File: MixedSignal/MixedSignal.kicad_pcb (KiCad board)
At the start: 4 copper layers, 103 x 75.5 mm, 106 parts, among them J1 PPPC202LFBN-RC, J2 PPPC202LFBN-RC, J4 Input Audio Jack, J5 SDS-50J, U1 ADG734, U10 ADG734, U10LDO1 TPS7A4901DGNR, U11 ADCMP602BRMZ, U12 ADCMP602BRMZ, U13 ADCMP602BRMZ, U14 ADCMP602BRMZ, U15 ADCMP602BRMZ, U16 ADCMP602BRMZ, U17 ADCMP602BRMZ, U18 CDCLVC1108PW, U19 DS90LV012ATMFX, U2 ADG734, U20 AP2112K-3.3TRG1, U3 ADG734, U4 WE-TVS-82400102 TVS Diode Arr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, U5 OPA1612AxD, U8 REF5025AD, U9 OPA1612AxD, U9LDO1 TPS7A3001DGN

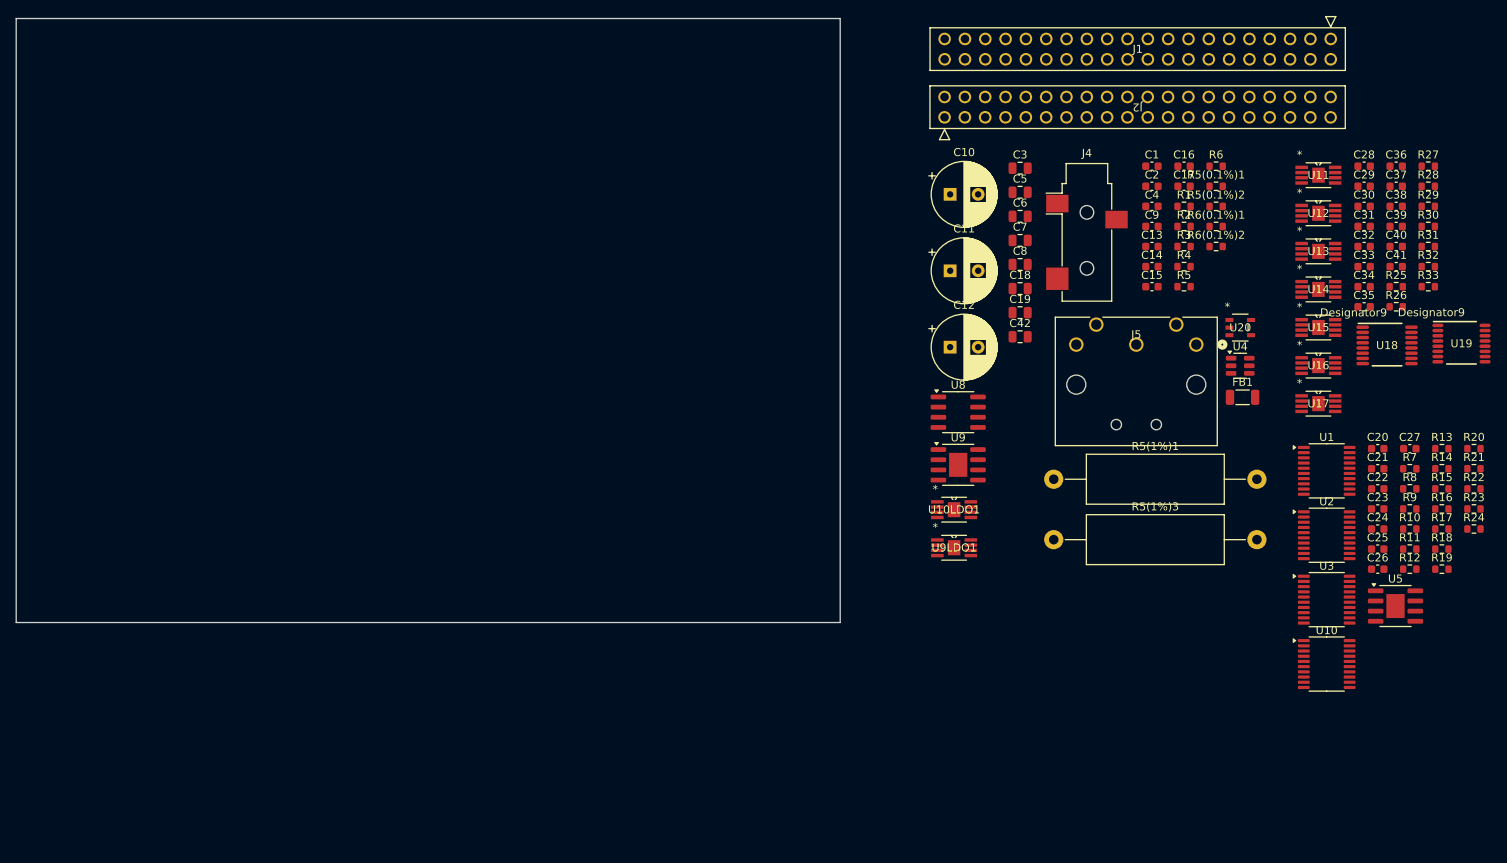
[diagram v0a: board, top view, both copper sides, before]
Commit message: passing DRC
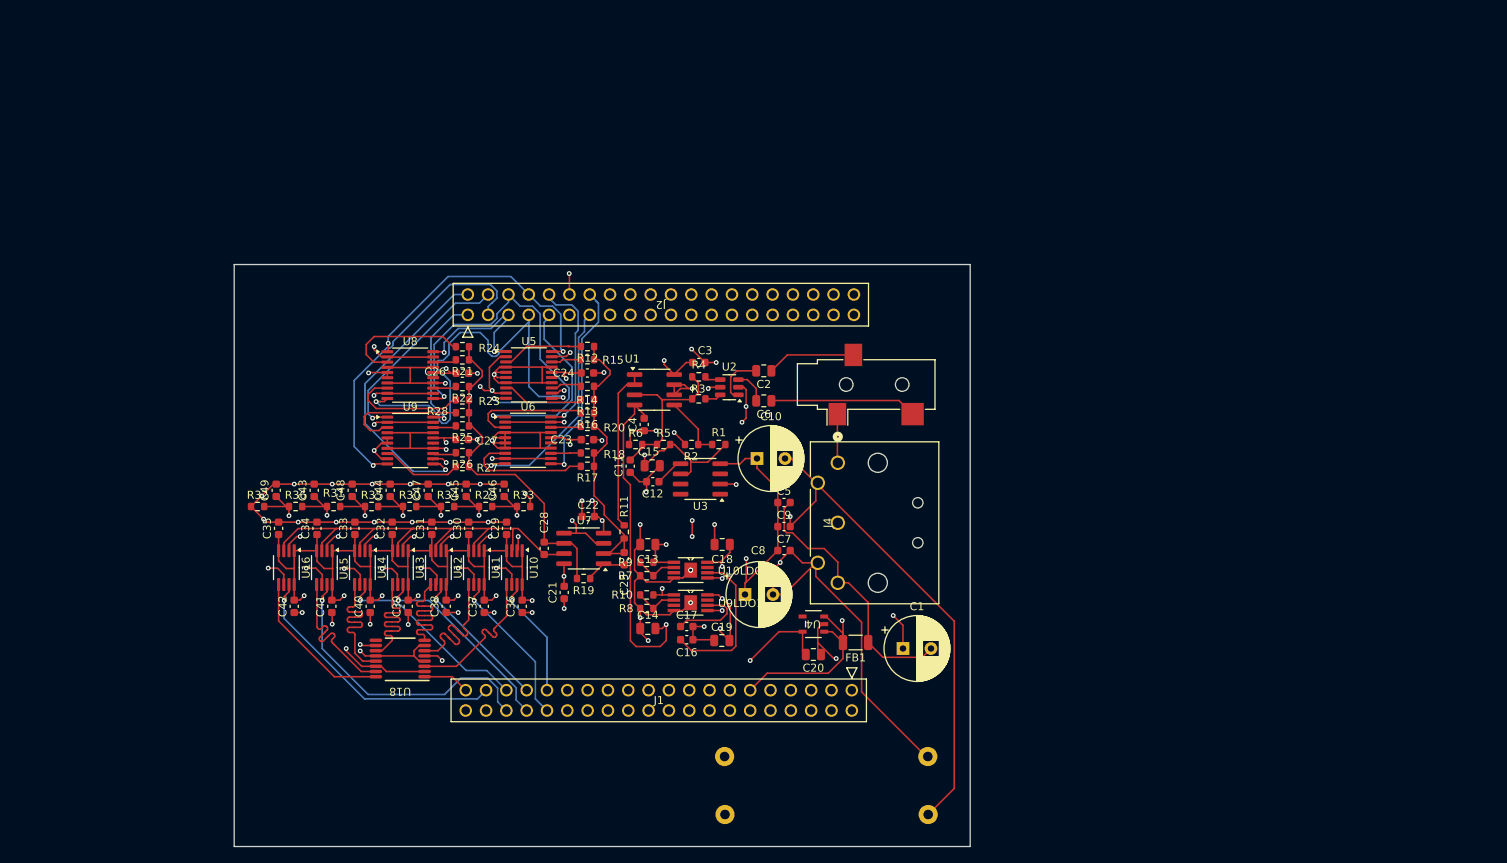
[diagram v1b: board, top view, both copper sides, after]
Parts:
- removed J5: SDS-50J, DIN5 Connector:CONN5_SDS-50J_CUD
- removed the R33 at (248.5, 70.5)
- removed R5(0.1%)1, R5(0.1%)2: 110k, Resistor_SMD:R_0603_1608Metric
- removed R5(1%)3: 150, 3W+ Load, move far from sensitive components, close to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, Resistor_THT:R_Axial_DIN0617_L17.0mm_D6.0mm_P25.40mm_Horizontal
- removed R6(0.1%)1, R6(0.1%)2: 12k, Resistor_SMD:R_0603_1608Metric
- removed U19: DS90LV012ATMFX, ClockDistributer:PW0016A_N
- removed U20: AP2112K-3.3TRG1, 3.3VLDO:SOT_RG1_DIO
- added C43: 0.1µF Ceramic, Capacitor_SMD:C_0603_1608Metric, F.Cu at (109.2, 96.0)
- added C44: 0.1µF Ceramic, Capacitor_SMD:C_0603_1608Metric, F.Cu at (118.8, 96.0)
- added C45: 0.1µF Ceramic, Capacitor_SMD:C_0603_1608Metric, F.Cu at (128.2, 96.0)
- added C46: 0.1µF Ceramic, Capacitor_SMD:C_0603_1608Metric, F.Cu at (133.0, 96.0)
- added C47: 0.1µF Ceramic, Capacitor_SMD:C_0603_1608Metric, F.Cu at (123.5, 96.0)
- added C48: 0.1µF Ceramic, Capacitor_SMD:C_0603_1608Metric, F.Cu at (114.0, 96.0)
- added C49: 0.1µF Ceramic, Capacitor_SMD:C_0603_1608Metric, F.Cu at (104.5, 96.0)
- added J4: SDS-50J, DIN5 Connector:CONN5_SDS-50J_CUD, F.Cu at (174.7, 92.5)
- added R10: 110k (0.1%), Resistor_SMD:R_0603_1608Metric, F.Cu at (150.8, 109.1)
- added R5(1%)2: 150, 3W+ Load, move far from sensitive components, close to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, Resistor_THT:R_Axial_DIN0617_L17.0mm_D6.0mm_P25.40mm_Horizontal, B.Cu at (186.0, 136.5)
- added R7: 12k (0.1%), Resistor_SMD:R_0603_1608Metric, F.Cu at (150.8, 106.6)
- added R8: 12k (0.1%), Resistor_SMD:R_0603_1608Metric, F.Cu at (150.8, 110.8)
- added R9: 110k (0.1%), Resistor_SMD:R_0603_1608Metric, F.Cu at (150.8, 105.0)
- added U4: AP2112K-3.3TRG1, 3.3VLDO:SOT_RG1_DIO, F.Cu at (171.6, 112.7)
- J1, J2: value PPPC202LFBN-RC -> ADAFRUIT 1992 (Tall)
- R5(1%)1: value 150, 3W+ Load, move far from sensitive components, close to port -> 150, 3W+ Load, move far from sensitive components, close to port, 1%; moved to B.Cu
- U1: renamed from U9; footprint Package_SO:SOIC-8-1EP_3.9x4.9mm_P1.27mm_EP2.29x3mm -> Package_SO:SOIC-8_3.9x4.9mm_P1.27mm
- U10: renamed from U11; footprint ADCComparator:DGN8_1P89X1P57 -> Package_SO:MSOP-8_3x3mm_P0.65mm
- U10LDO1, U9LDO1: footprint ADCComparator:DGN8_1P89X1P57 -> TPS7A49:DGN8_1P89X1P57
- U11: renamed from U12; footprint ADCComparator:DGN8_1P89X1P57 -> Package_SO:MSOP-8_3x3mm_P0.65mm
- U12: renamed from U13; footprint ADCComparator:DGN8_1P89X1P57 -> Package_SO:MSOP-8_3x3mm_P0.65mm
- U13: renamed from U14; footprint ADCComparator:DGN8_1P89X1P57 -> Package_SO:MSOP-8_3x3mm_P0.65mm
- U14: renamed from U15; footprint ADCComparator:DGN8_1P89X1P57 -> Package_SO:MSOP-8_3x3mm_P0.65mm
- U15: renamed from U16; footprint ADCComparator:DGN8_1P89X1P57 -> Package_SO:MSOP-8_3x3mm_P0.65mm
- U16: renamed from U17; footprint ADCComparator:DGN8_1P89X1P57 -> Package_SO:MSOP-8_3x3mm_P0.65mm
- U7: renamed from U5; footprint Package_SO:SOIC-8-1EP_3.9x4.9mm_P1.27mm_EP2.29x3mm -> Package_SO:SOIC-8_3.9x4.9mm_P1.27mm
- moved R32 149.4 mm to (102.2, 98.0)
- moved R36 145.3 mm to (106.9, 98.0)
- moved C42 144.1 mm to (106.8, 110.5), turned to 90 degrees
- moved C35 144.1 mm to (104.8, 100.7), turned to 90 degrees
- moved C41 141.3 mm to (111.5, 110.5), turned to 90 degrees
- moved R31 141.2 mm to (111.7, 98.0)
- moved C34 140.8 mm to (109.6, 100.7), turned to 90 degrees
- moved C40 138.6 mm to (116.2, 110.5), turned to 90 degrees
- moved C33 137.8 mm to (114.3, 100.7), turned to 90 degrees
- moved R35 137.3 mm to (116.4, 98.0)
- moved R30 133.5 mm to (121.2, 98.0)
- moved U16 130.6 mm to (105.8, 105.6), turned to -90 degrees
- moved R34 129.8 mm to (125.9, 98.0)
- moved U18 129.4 mm to (120.0, 117.0), turned to 180 degrees
- moved R28 127.3 mm to (127.8, 86.3), turned to 180 degrees
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- renumbered C11 to C1, C12 to C10, C16 to C11, C9 to C12, C5 to C13, C3 to C14, C8 to C15, C4 to C16, C2 to C17, C7 to C18, C6 to C19, C18 to C2, C42 to C20, C20 to C21, C21 to C22, C24 to C23, C25 to C24, C22 to C25, C23 to C28, C28 to C29, C1 to C3, C32 to C31, C34 to C32, C36 to C33, C38 to C34, C40 to C35, C29 to C36, C31 to C37, C33 to C38, C35 to C39, C17 to C4, C37 to C40, C39 to C41, C41 to C42, C13 to C5, C19 to C6, C14 to C7, C10 to C8, C15 to C9, J4 to J3, R6 to R1, R7 to R11, R9 to R12, R10 to R13, R11 to R14, R12 to R15, R13 to R16, R14 to R17, R15 to R18, R8 to R19, R5 to R2, R16 to R20, R17 to R21, R18 to R22, R19 to R23, R20 to R24, R21 to R25, R22 to R26, R23 to R27, R24 to R28, R26 to R29, R1 to R3, R28 to R30, R30 to R31, R25 to R33, R27 to R34, R29 to R35, R31 to R36, R2 to R4, R3 to R5, R4 to R6, U4 to U2, U8 to U3, U1 to U5, U2 to U6, U3 to U8, U10 to U9
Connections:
- C27 pad 1: GND -> 3.3V
- C27 pad 2: 3.3V -> GND
- J1 pad 21: LVDS+ -> unconnected-(J1-Pad21)
- J1 pad 22: LVDS- -> unconnected-(J1-Pad22)
- J1 pad 39: unconnected-(J1-Pad39) -> ComparatorClock
- J2 pad 1: DAC_CTRL_1 -> DAC_CTRL_5
- J2 pad 10: unconnected-(J2-Pad10) -> DAC_CTRL_8
- J2 pad 13: unconnected-(J2-Pad13) -> DAC_CTRL_6
- J2 pad 14: unconnected-(J2-Pad14) -> DAC_CTRL_7
- J2 pad 2: DAC_CTRL_2 -> DAC_CTRL_6
- J2 pad 3: DAC_CTRL_3 -> DAC_CTRL_7
- J2 pad 4: DAC_CTRL_4 -> DAC_CTRL_8
- J2 pad 5: DAC_CTRL_5 -> DAC_CTRL_1
- J2 pad 6: DAC_CTRL_6 -> DAC_CTRL_2
- J2 pad 7: DAC_CTRL_7 -> DAC_CTRL_3
- J2 pad 8: DAC_CTRL_8 -> DAC_CTRL_4
- J2 pad 9: unconnected-(J2-Pad9) -> DAC_CTRL_5
- U18 pad 1: PostRecieveClk -> ComparatorClock
- U18 pad 11: Clk_PostFanout_6 -> Clk_PostFanout_4
- U18 pad 13: Clk_PostFanout_3 -> Clk_PostFanout_5
- U18 pad 15: Clk_PostFanout_4 -> Clk_PostFanout_6
- U18 pad 16: Clk_PostFanout_2 -> Clk_PostFanout_7
- U18 pad 6: Clk_PostFanout_5 -> Clk_PostFanout_2
- U18 pad 8: Clk_PostFanout_7 -> Clk_PostFanout_3
- U8 pad 1: DAC_CTRL_1 -> DAC_CTRL_4
- U8 pad 10: DAC_CTRL_2 -> DAC_CTRL_3
- U8 pad 11: DAC_CTRL_3 -> DAC_CTRL_2
- U8 pad 13: FB_2.3 -> FB_2.2
- U8 pad 18: FB_2.4 -> FB_2.1
- U8 pad 20: DAC_CTRL_4 -> DAC_CTRL_1
- U8 pad 3: FB_2.1 -> FB_2.4
- U8 pad 8: FB_2.2 -> FB_2.3
- U9 pad 1: DAC_CTRL_5 -> DAC_CTRL_8
- U9 pad 10: DAC_CTRL_6 -> DAC_CTRL_7
- U9 pad 11: DAC_CTRL_7 -> DAC_CTRL_6
- U9 pad 13: FB_2.7 -> FB_2.6
- U9 pad 18: FB_2.8 -> FB_2.5
- U9 pad 20: DAC_CTRL_8 -> DAC_CTRL_5
- U9 pad 3: FB_2.5 -> FB_2.8
- U9 pad 8: FB_2.6 -> FB_2.7
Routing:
- net 3.3V: track 0.00 -> 323.0 mm, vias 0 -> 15
- net GND: track 0.00 -> 307.4 mm, vias 0 -> 62
- net +2.5V: track 0.00 -> 169.6 mm, vias 0 -> 10
- net -15V: track 0.00 -> 98.4 mm, vias 0 -> 4
- net 5V: track 0.00 -> 93.8 mm, vias 0 -> 2
- net +1.25V: track 0.00 -> 85.3 mm, vias 0 -> 6
- net +12V: track 0.00 -> 76.0 mm, vias 0 -> 4
- net -12V: track 0.00 -> 72.8 mm, vias 0 -> 4
- net DAC_CTRL_7: track 0.00 -> 65.9 mm, vias 0 -> 2
- net DAC_CTRL_6: track 0.00 -> 65.7 mm, vias 0 -> 2
- net +15V: track 0.00 -> 65.3 mm, vias 0 -> 3
- net /Analog Frontend/3b Flash ADC/Flash ADC Input: track 0.00 -> 59.7 mm
- net DAC_CTRL_3: track 0.00 -> 56.2 mm, vias 0 -> 2
- net DAC_CTRL_2: track 0.00 -> 49.6 mm, vias 0 -> 2
- net DAC_CTRL_8: track 0.00 -> 45.8 mm, vias 0 -> 2
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- added copper zone on In1.Cu, net GND
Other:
- board size 103 x 75.5 mm -> 92 x 72.8 mm

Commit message: board rev. 1.1
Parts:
- removed R20: 16.9k, Resistor_SMD:R_0603_1608Metric
- removed R28: 13k, Resistor_SMD:R_0603_1608Metric
- added C50: 0.1µF Ceramic, Capacitor_SMD:C_0603_1608Metric, F.Cu at (114.8, 113.2)
- added C51: 0.1µF Ceramic, Capacitor_SMD:C_0603_1608Metric, F.Cu at (126.8, 116.8)
- added C52: 0.1µF Ceramic, Capacitor_SMD:C_0603_1608Metric, F.Cu at (112.8, 117.5)
- added C53: 0.1µF Ceramic, Capacitor_SMD:C_0603_1608Metric, F.Cu at (162.2, 96.5)
- added C54: 0.1µF Ceramic, Capacitor_SMD:C_0603_1608Metric, F.Cu at (140.2, 98.2)
- added C55: 0.1µF Ceramic, Capacitor_SMD:C_0603_1608Metric, F.Cu at (114.9, 85.8)
- added C56: 0.1µF Ceramic, Capacitor_SMD:C_0603_1608Metric, F.Cu at (127.8, 86.3)
- added C57: 0.1µF Ceramic, Capacitor_SMD:C_0603_1608Metric, F.Cu at (131.0, 86.5)
- added C58: 0.1µF Ceramic, Capacitor_SMD:C_0603_1608Metric, F.Cu at (143.4, 86.3)
- added C59: 10µF Ceramic, Capacitor_SMD:C_0805_2012Metric, F.Cu at (114.7, 82.0)
- added C60: 10µF Ceramic, Capacitor_SMD:C_0805_2012Metric, F.Cu at (142.6, 95.0)
- added C61: 0.1µF Ceramic, Capacitor_SMD:C_0603_1608Metric, F.Cu at (139.0, 76.8)
- added C62: 0.1µF Ceramic, Capacitor_SMD:C_0603_1608Metric, F.Cu at (138.8, 95.2)
- added D1: STATUS, Diode_SMD:D_0603_1608Metric, F.Cu at (138.8, 116.2)
- added D2: STATUS, Diode_SMD:D_0603_1608Metric, F.Cu at (138.8, 113.0)
- added FB2: Ferrite Bead, Diode_SMD:D_0603_1608Metric, F.Cu at (165.6, 78.5)
- added G***: LOGO, LOGO, F.Cu at (143.0, 132.5)
- added G***: LOGO, LOGO, F.Cu at (145.0, 132.5)
- added G***: LOGO, LOGO, F.Cu at (186.2, 132.5)
- added G***: LOGO, LOGO, F.Cu at (145.5, 132.5)
- added G***: LOGO, LOGO, F.Cu at (188.0, 132.5)
- added G***: LOGO, LOGO, F.Cu at (167.5, 132.5)
- added G***: LOGO, LOGO, F.Cu at (190.0, 132.5)
- added G***: LOGO, LOGO, F.Cu at (143.8, 132.5)
- added G***: LOGO, LOGO, F.Cu at (140.5, 132.5)
- added G***: LOGO, LOGO, F.Cu at (191.2, 132.5)
- added G***: LOGO, LOGO, F.Cu at (148.0, 132.5)
- added G***: LOGO, LOGO, F.Cu at (146.2, 132.5)
- added G***: LOGO, LOGO, F.Cu at (144.2, 132.5)
- added G***: LOGO, LOGO, F.Cu at (141.8, 132.5)
- added G***: LOGO, LOGO, F.Cu at (165.5, 132.5)
- added G***: LOGO, LOGO, F.Cu at (170.0, 132.5)
- added G***: LOGO, LOGO, F.Cu at (185.0, 132.5)
- added G***: LOGO, LOGO, F.Cu at (170.5, 132.5)
- added G***: LOGO, LOGO, F.Cu at (169.2, 132.5)
- added G***: LOGO, LOGO, F.Cu at (146.8, 132.5)
- added G***: LOGO, LOGO, F.Cu at (164.2, 132.5)
- added G***: LOGO, LOGO, F.Cu at (193.0, 132.5)
- added G***: LOGO, LOGO, F.Cu at (192.5, 132.5)
- added G***: LOGO, LOGO, F.Cu at (168.0, 132.5)
- added G***: LOGO, LOGO, F.Cu at (163.0, 132.5)
- added G***: LOGO, LOGO, F.Cu at (147.5, 132.5)
- added G***: LOGO, LOGO, F.Cu at (190.5, 132.5)
- added G***: LOGO, LOGO, F.Cu at (185.5, 132.5)
- added G***: LOGO, LOGO, F.Cu at (186.8, 132.5)
- added G***: LOGO, LOGO, F.Cu at (165.0, 132.5)
- added G***: LOGO, LOGO, F.Cu at (187.5, 132.5)
- added G***: LOGO, LOGO, F.Cu at (189.2, 132.5)
- added G***: LOGO, LOGO, F.Cu at (163.8, 132.5)
- added G***: LOGO, LOGO, F.Cu at (166.2, 132.5)
- added G***: LOGO, LOGO, F.Cu at (142.5, 132.5)
- added G***: LOGO, LOGO, F.Cu at (168.8, 132.5)
- added G***: LOGO, LOGO, F.Cu at (188.8, 132.5)
- added G***: LOGO, LOGO, F.Cu at (191.8, 132.5)
- added G***: LOGO, LOGO, F.Cu at (166.8, 132.5)
- added G***: LOGO, LOGO, F.Cu at (141.2, 132.5)
- added G***: LOGO, LOGO, F.Cu at (140.0, 132.5)
- added G***: LOGO, LOGO, F.Cu at (162.5, 132.5)
- added J5: B2B-XH-ALFSN, B2BHeader:CONN_B2B-XH-ALFSN_JST, F.Cu at (184.6, 73.6)
- added REF**: MountingHole_3.2mm_M3, MountingHole:MountingHole_3.2mm_M3, F.Cu at (185.6, 122.2)
- added REF**: MountingHole_3.2mm_M3, MountingHole:MountingHole_3.2mm_M3, F.Cu at (111.7, 72.5)
- C1: value 100µF Electrolytic (25V) -> 100µF Electrolytic
- C10, C8: value 100µF Electrolytic (25V) close to port -> 100µF Electrolytic
- C13, C14, C18, C19, C2, C6: value 10µF X7R Ceramic -> 10µF Ceramic
- C16, C17: value 50nF -> 0.1µF Ceramic
- C25, C28: value 47pF -> 100pF
- FB1: value FerriteBead -> Ferrite Bead; footprint Inductor_SMD:L_1206_3216Metric -> Diode_SMD:D_0603_1608Metric
- J4: value SDS-50J -> DIN5 Connector
- R1, R2: value 1k(0.1%) -> 10k
- R10, R9: value 110k (0.1%) -> 100k
- R11: value 2.8k -> 1.5k
- R12, R13, R14, R15, R16, R17, R18: value 16.9k -> 14k
- R19: value 1.62k -> 1.5k
- R21, R22, R23, R24, R25, R26, R27: value 13k -> 7.32k
- R29, R30, R31, R32, R33, R34, R35, R36: value 100(0.1%) -> 100
- R3, R4: value 100 -> 13k
- R37: renamed from R5(1%)1; value 150, 3W+ Load, move far from sensitive components, close to port, 1% -> 150
- R38: renamed from R5(1%)2; value 150, 3W+ Load, move far from sensitive components, close to port, 1% -> 150
- R7, R8: value 12k (0.1%) -> 12k
- U9LDO1: value TPS7A3001DGN -> TPS7A3001DGNR
- moved R2 29.5 mm to (142.6, 116.2)
- moved R1 28.6 mm to (142.6, 113.0)
- moved C5 16.6 mm to (176.0, 112.0), turned to 90 degrees
- moved FB1 4.76 mm to (172.5, 116.8)
- moved C20 3.85 mm to (167.8, 116.5)
- moved C9 3.73 mm to (169.2, 97.0)
- moved C1 3.67 mm to (179.2, 115.0)
- moved R16 1.67 mm to (143.4, 88.0)
- moved C7 1.37 mm to (169.2, 104.0)
- moved U4 1.05 mm to (170.8, 113.2)
- moved C18 0.84 mm to (161.1, 103.0), turned to 180 degrees
- moved C2 0.46 mm to (165.4, 81.5)
- moved J1 0.23 mm to (176.4, 121.2)
- moved J2 0.23 mm to (128.4, 73.8)
- moved C41 0.20 mm to (111.2, 110.5)
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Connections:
- J1 pad 27: unconnected-(J1-Pad27) -> ComparatorClock
- J1 pad 39: ComparatorClock -> unconnected-(J1-Pad39)
- J2 pad 1: DAC_CTRL_5 -> DAC_CTRL_5B
- J2 pad 10: DAC_CTRL_8 -> unconnected-(J2-Pad10)
- J2 pad 13: DAC_CTRL_6 -> DAC_CTRL_6A
- J2 pad 14: DAC_CTRL_7 -> DAC_CTRL_7A
- J2 pad 2: DAC_CTRL_6 -> DAC_CTRL_6B
- J2 pad 3: DAC_CTRL_7 -> DAC_CTRL_7B
- J2 pad 4: DAC_CTRL_8 -> unconnected-(J2-Pad4)
- J2 pad 9: DAC_CTRL_5 -> DAC_CTRL_5A
- R1 pad 1: Net-(U1B-+) -> Net-(D2-K)
- R1 pad 2: +2.5V -> -15V
- R2 pad 1: GND -> Net-(D1-A)
- R2 pad 2: Net-(U1B-+) -> +15V
- U1 pad 5: Net-(U1B-+) -> +1.25V
- U1 pad 6: +1.25V -> Net-(U1B--)
- U1 pad 7: +1.25V -> Net-(U1B--)
- U6 pad 1: DAC_CTRL_5 -> GND
- U6 pad 10: DAC_CTRL_6 -> DAC_CTRL_6A
- U6 pad 11: DAC_CTRL_7 -> DAC_CTRL_7A
- U6 pad 18: FB_1.8 -> FB_1.5
- U6 pad 2: +2.5V -> GND
- U6 pad 20: DAC_CTRL_8 -> DAC_CTRL_5A
- U6 pad 3: FB_1.5 -> GND
- U9 pad 1: DAC_CTRL_8 -> GND
- U9 pad 10: DAC_CTRL_7 -> DAC_CTRL_7B
- U9 pad 11: DAC_CTRL_6 -> DAC_CTRL_6B
- U9 pad 20: DAC_CTRL_5 -> DAC_CTRL_5B
- U9 pad 3: FB_2.8 -> GND
- U9 pad 4: +2.5V -> GND
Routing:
- net DAC_CTRL_7: track 65.9 -> 0.00 mm, vias 2 -> 0
- net DAC_CTRL_6: track 65.7 -> 0.00 mm, vias 2 -> 0
- net DAC_CTRL_8: track 45.8 -> 0.00 mm, vias 2 -> 0
- net DAC_CTRL_5: track 42.8 -> 0.00 mm, vias 2 -> 0
- net DAC_CTRL_7B: track 0.00 -> 40.6 mm, vias 0 -> 1
- net +2.5V: track 169.6 -> 207.2 mm, vias 10 -> 13
- net DAC_CTRL_6B: track 0.00 -> 37.5 mm, vias 0 -> 1
- net GND: track 307.4 -> 342.6 mm, vias 62 -> 185
- net +15V: track 65.3 -> 99.0 mm
- net DAC_CTRL_6A: track 0.00 -> 28.7 mm, vias 0 -> 1
- net DAC_CTRL_7A: track 0.00 -> 25.6 mm, vias 0 -> 1
- net -15V: track 98.4 -> 119.4 mm, vias 4 -> 5
- net 5VOut: track 0.00 -> 20.7 mm
- net DAC_CTRL_5B: track 0.00 -> 17.8 mm, vias 0 -> 1
- net FB_2.8: track 16.3 -> 0.00 mm
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- added copper zone on In2.Cu, net +1.25V
- added copper zone on In2.Cu, net +12V
- added copper zone on In2.Cu, net +15V
- added copper zone on In2.Cu, net +2.5V
- added copper zone on In2.Cu, net -12V
- added copper zone on In2.Cu, net -15V
- added copper zone on In2.Cu, net 3.3V
- added copper zone on In2.Cu, net 5V
- added copper zone on B.Cu, net GND
- added copper zone on F.Cu, net GND
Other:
- board text added: "2nd-Order CIFB CT ΔΣ"
- board text added: "3-Bit Flash ADC | Rev. 1.1"
- board text added: "Magellan"
- board text added: "The Works of Man"
- board text added: "し"
- board text added: "の"
- board text added: "も"
- board text added: "り"
- board text added: "人"
- board text added: "造"
